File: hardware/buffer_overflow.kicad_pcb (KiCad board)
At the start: 2 copper layers, 33.1 x 30.1 mm, 19 parts, among them J1 E1, U1 LM741

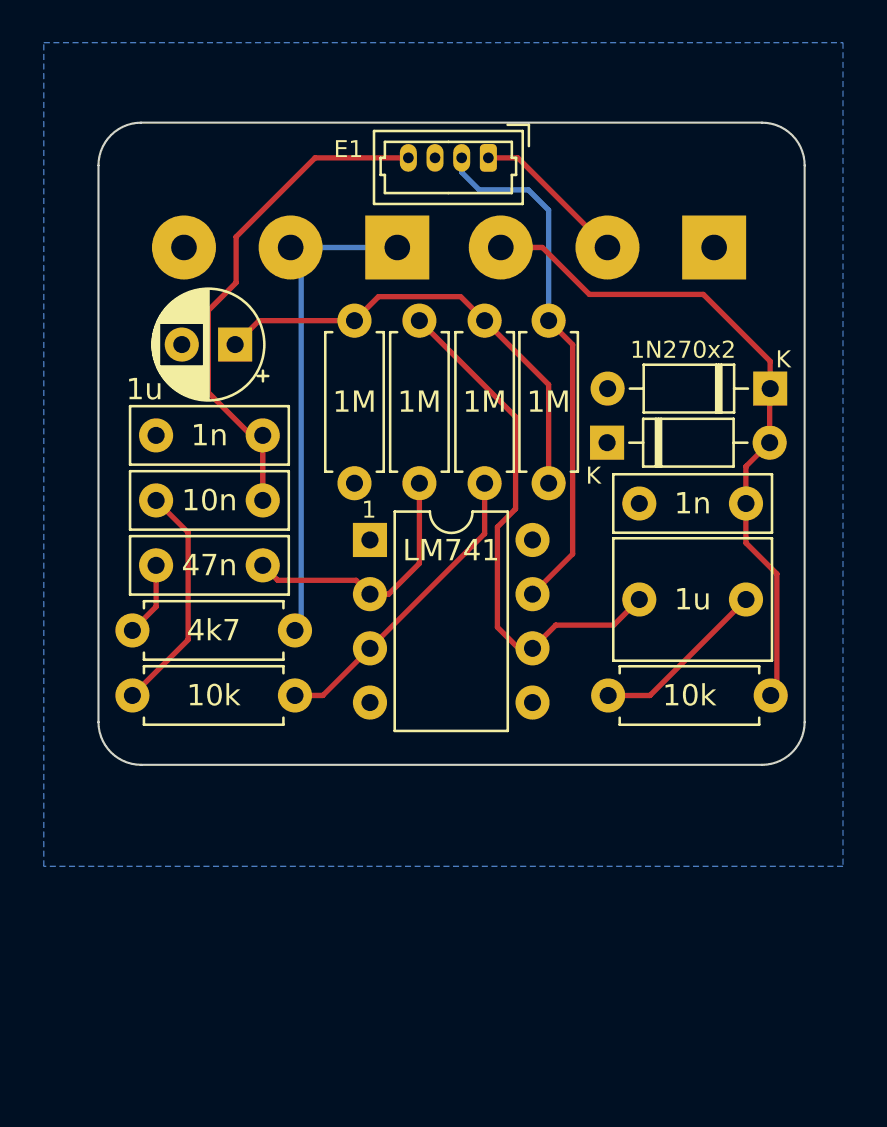
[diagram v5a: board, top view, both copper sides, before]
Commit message: Some updates based on feedback from freestompboxes.org folks:
 - Add back thermal reliefs on ground pads
 - Switch to stereo jacks for improved mechanical support
 - Add 3D models for various parts (courtesy of Vasily Kashirin - https://grabcad.com/vasily.kashirin-1/models?page=1)
 - Add more space between potentiometers (need to update the courtyard to make this more obvious in the future)
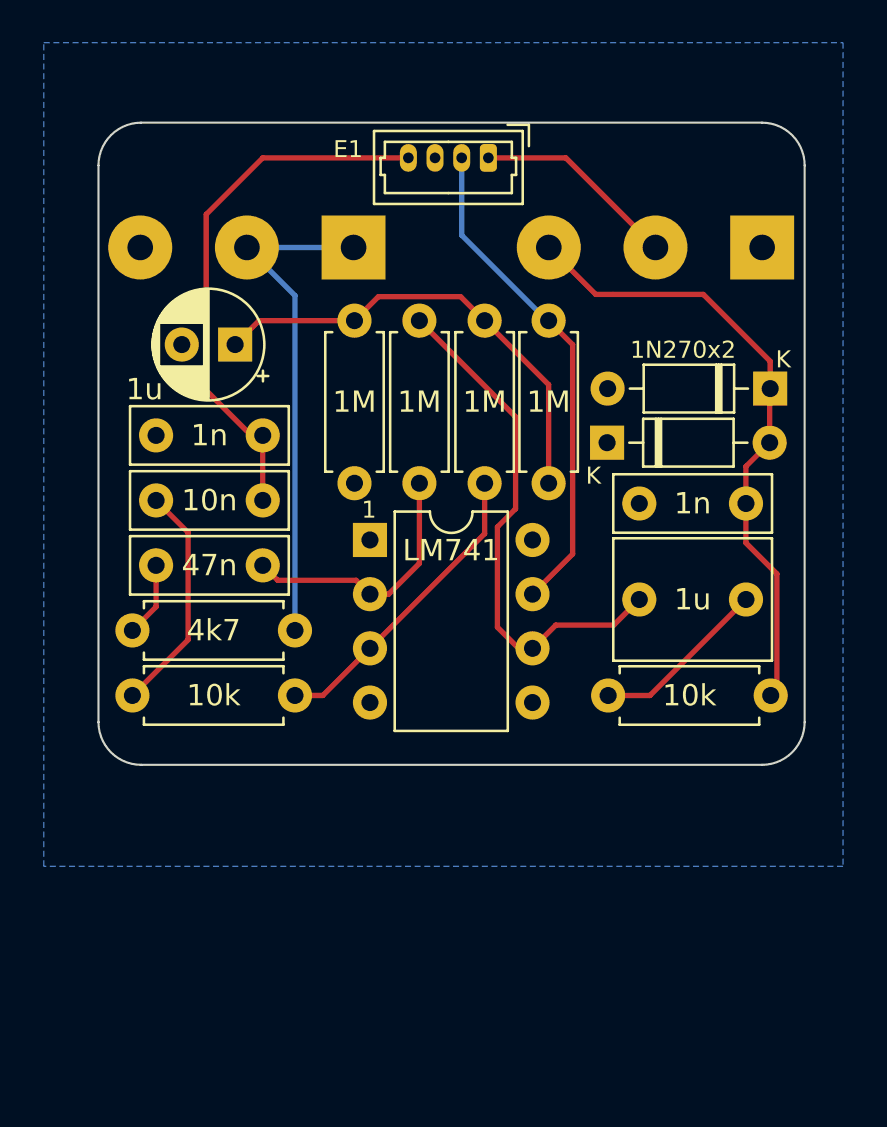
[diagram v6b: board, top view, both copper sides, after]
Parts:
- J1: footprint Connector_Molex:Molex_PicoBlade_53047-0410_1x04_P1.25mm_Vertical -> buffer_overflow:Molex_PicoBlade_53047-0410_1x04_P1.25mm_Vertical_with_3D_Model
- moved POT1 2.25 mm to (71.2, 29.6)
- moved POT2 2.05 mm to (52.0, 29.6)
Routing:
- net /EFFECT_OUT: track 7.32 -> 9.57 mm
- net /PRE_VOLUME: track 31.7 -> 29.5 mm
- net /EFFECT_IN: track 23.9 -> 25.4 mm
- net /9V0: track 24.7 -> 23.4 mm
- net /GAIN_CTL: track 23.4 -> 24.6 mm
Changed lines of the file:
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@@
   (title_block
     (title "Buffer Overflow Drive Effect")
-    (date "2023-03-03")
-    (rev "v0.38")
+    (date "2023-03-04")
+    (rev "v0.39")
     (comment 1 " github.com/whbeers/buffer_overflow")
   )
@@
     )
   )
-  (footprint "Connector_Molex:Molex_PicoBlade_53047-0410_1x04_P1.25mm_Vertical" (layer "F.Cu")
+  (footprint "buffer_overflow:Molex_PicoBlade_53047-0410_1x04_P1.25mm_Vertical_with_3D_Model" (layer "F.Cu")
     (at 63.375 29.25 180)
     (descr "Molex PicoBlade Connector System, 53047-0410, 4 Pins per row (http://www.molex.com/pdm_docs/sd/530470610_sd.pdf), generated with kicad-footprint-generator")
@@
     (property "ki_keywords" "connector")
     (attr through_hole)
-    (fp_text reference "J1" (at 1.88 -3.25) (layer "F.Fab")
-        (effects (font (size 1 1) (thickness 0.15)))
-    )
-    (fp_text value "E1" (at 6.555113 0.399999) (layer "F.SilkS" knockout)
+    (fp_text reference "J1" (at 1.88 -3.25 180) (layer "F.Fab")
+        (effects (font (size 1 1) (thickness 0.15)))
+    )
+    (fp_text value "E1" (at 6.575 0.4 180) (layer "F.SilkS" knockout)
         (effects (font (size 0.8 0.8) (thickness 0.15)))
     )
-    (fp_text user "${REFERENCE}" (at 1.88 -1.35) (layer "F.Fab")
+    (fp_text user "${REFERENCE}" (at 1.88 -1.35 180) (layer "F.Fab")
         (effects (font (size 1 1) (thickness 0.15)))
     )
@@
       (rotate (xyz 0 0 0))
     )
+    (model "/home/whbeers/src-mine/stepfiles/530470410.stp"
+      (offset (xyz 1.9 -1.15 5.5))
+      (scale (xyz 1 1 1))
+      (rotate (xyz 90 0 0))
+    )
   )
   (footprint "Resistor_THT:R_Axial_DIN0207_L6.3mm_D2.5mm_P7.62mm_Horizontal" (layer "F.Cu")
@@
   )
   (footprint "buffer_overflow:Potentiometer_Single_3_Horizontal" (layer "B.Cu")
-    (at 68.95 29.64 180)
+    (at 71.2 29.64 180)
     (property "Label" "Volume")
     (property "Sheetfile" "buffer_overflow.kicad_sch")
@@
     (property "ki_keywords" "resistor variable")
     (attr through_hole)
-    (fp_text reference "POT1" (at -0.0075 -7.06 unlocked) (layer "B.Fab" knockout)
+    (fp_text reference "POT1" (at -0.0075 -7.06 unlocked) (layer "B.Fab")
         (effects (font (size 1 1) (thickness 0.15)) (justify mirror))
     )
@@
         (effects (font (size 0.8 0.8) (thickness 0.15)) (justify mirror))
     )
-    (fp_text user "Vol" (at -7.75 -4.41 270 unlocked) (layer "B.SilkS" knockout)
+    (fp_text user "Vol" (at -5.5 -6.61 unlocked) (layer "B.SilkS" knockout)
         (effects (font (size 0.8 0.8) (thickness 0.15)) (justify mirror))
     )
@@
     (pad "3" thru_hole circle (at 4.9925 -3.81 270) (size 3 3) (drill 1.2) (layers "*.Cu" "*.Mask")
       (net 9 "/PRE_VOLUME") (pinfunction "3") (pintype "passive"))
+    (model "/home/whbeers/src-mine/stepfiles/RV16AF-41.step"
+      (offset (xyz 0 12.2 0.5))
+      (scale (xyz 1 1 1))
+      (rotate (xyz 0 0 0))
+    )
   )
   (footprint "buffer_overflow:Potentiometer_Single_3_Horizontal" (layer "B.Cu")
-    (at 54.1 29.64 180)
+    (at 52.05 29.64 180)
     (property "Label" "Gain")
     (property "Sheetfile" "buffer_overflow.kicad_sch")
@@
     (property "ki_keywords" "resistor variable")
     (attr through_hole)
-    (fp_text reference "POT2" (at 0 -7.06 unlocked) (layer "B.Fab" knockout)
+    (fp_text reference "POT2" (at 0 -7.06 unlocked) (layer "B.Fab")
         (effects (font (size 1 1) (thickness 0.15)) (justify mirror))
     )
@@
         (effects (font (size 0.8 0.8) (thickness 0.15)) (justify mirror))
     )
-    (fp_text user "Gain" (at 7.65 -3.61 90 unlocked) (layer "B.SilkS" knockout)
+    (fp_text user "Gain" (at 5.1 -6.56 unlocked) (layer "B.SilkS" knockout)
         (effects (font (size 0.8 0.8) (thickness 0.15)) (justify mirror))
     )
@@
     (pad "3" thru_hole circle (at 4.9925 -3.81 270) (size 3 3) (drill 1.2) (layers "*.Cu" "*.Mask")
       (net 1 "GND") (pinfunction "3") (pintype "passive"))
+    (model "/home/whbeers/src-mine/stepfiles/RV16AF-41.step"
+      (offset (xyz 0 12.2 0.5))
+      (scale (xyz 1 1 1))
+      (rotate (xyz 0 0 0))
+    )
   )
   (gr_arc (start 45.1 29.6) (mid 45.685786 28.185786) (end 47.1 27.6)
@@
   (segment (start 70.95 54.45) (end 75.45 49.95) (width 0.25) (layer "F.Cu") (net 4))
   (segment (start 68.99 54.45) (end 70.95 54.45) (width 0.25) (layer "F.Cu") (net 4))
-  (segment (start 51.55 32.95) (end 51.55 35.1) (width 0.25) (layer "F.Cu") (net 5))
-  (segment (start 50.25 36.4) (end 50.25 40.25) (width 0.25) (layer "F.Cu") (net 5))
+  (segment (start 59.625 29.25) (end 52.8 29.25) (width 0.25) (layer "F.Cu") (net 5))
+  (segment (start 50.15 31.9) (end 50.15 40.15) (width 0.25) (layer "F.Cu") (net 5))
   (segment (start 52.8 42.258) (end 52.8 45.306) (width 0.25) (layer "F.Cu") (net 5))
-  (segment (start 51.55 35.1) (end 50.25 36.4) (width 0.25) (layer "F.Cu") (net 5))
-  (segment (start 55.25 29.25) (end 51.55 32.95) (width 0.25) (layer "F.Cu") (net 5))
-  (segment (start 59.625 29.25) (end 55.25 29.25) (width 0.25) (layer "F.Cu") (net 5))
-  (segment (start 50.25 40.25) (end 52.258 42.258) (width 0.25) (layer "F.Cu") (net 5))
+  (segment (start 52.8 29.25) (end 50.15 31.9) (width 0.25) (layer "F.Cu") (net 5))
   (segment (start 52.258 42.258) (end 52.8 42.258) (width 0.25) (layer "F.Cu") (net 5))
+  (segment (start 50.15 40.15) (end 52.258 42.258) (width 0.25) (layer "F.Cu") (net 5))
   (segment (start 46.69 54.448) (end 49.3 51.838) (width 0.25) (layer "F.Cu") (net 6))
   (segment (start 49.3 51.838) (end 49.3 46.806) (width 0.25) (layer "F.Cu") (net 6))
@@
   (segment (start 66.535 51.15) (end 65.445 52.24) (width 0.25) (layer "F.Cu") (net 8))
   (segment (start 64.65 45.7) (end 63.8 46.55) (width 0.25) (layer "F.Cu") (net 8))
-  (segment (start 65.909009 33.45) (end 63.9575 33.45) (width 0.25) (layer "F.Cu") (net 9))
   (segment (start 73.45 35.65) (end 76.585 38.785) (width 0.25) (layer "F.Cu") (net 9))
   (segment (start 76.56 40.09) (end 76.585 40.065) (width 0.25) (layer "F.Cu") (net 9))
   (segment (start 75.45 45.45) (end 75.45 47.3) (width 0.25) (layer "F.Cu") (net 9))
+  (segment (start 66.2075 33.45) (end 68.4075 35.65) (width 0.25) (layer "F.Cu") (net 9))
   (segment (start 76.56 42.6) (end 76.56 40.09) (width 0.25) (layer "F.Cu") (net 9))
   (segment (start 76.585 38.785) (end 76.585 40.065) (width 0.25) (layer "F.Cu") (net 9))
-  (segment (start 73.45 35.65) (end 68.109009 35.65) (width 0.25) (layer "F.Cu") (net 9))
+  (segment (start 68.4075 35.65) (end 69.2 35.65) (width 0.25) (layer "F.Cu") (net 9))
   (segment (start 75.45 43.71) (end 75.45 45.45) (width 0.25) (layer "F.Cu") (net 9))
+  (segment (start 73.45 35.65) (end 69.2 35.65) (width 0.25) (layer "F.Cu") (net 9))
   (segment (start 76.56 42.6) (end 75.45 43.71) (width 0.25) (layer "F.Cu") (net 9))
   (segment (start 76.9 48.75) (end 76.9 54.2) (width 0.25) (layer "F.Cu") (net 9))
@@
   (segment (start 76.9 54.2) (end 76.65 54.45) (width 0.25) (layer "F.Cu") (net 9))
   (segment (start 76.61 54.45) (end 76.65 54.45) (width 0.25) (layer "F.Cu") (net 9))
-  (segment (start 68.109009 35.65) (end 65.909009 33.45) (width 0.25) (layer "F.Cu") (net 9))
+  (segment (start 52.0575 33.45) (end 57.0575 33.45) (width 0.25) (layer "B.Cu") (net 10))
   (segment (start 54.6 50.912) (end 54.11 51.402) (width 0.25) (layer "B.Cu") (net 10))
-  (segment (start 54.1075 33.45) (end 54.6 33.9425) (width 0.25) (layer "B.Cu") (net 10))
-  (segment (start 59.1075 33.45) (end 54.1075 33.45) (width 0.25) (layer "B.Cu") (net 10))
-  (segment (start 54.6 33.9425) (end 54.6 50.912) (width 0.25) (layer "B.Cu") (net 10))
+  (segment (start 54.31 51.4) (end 54.31 35.7025) (width 0.25) (layer "B.Cu") (net 10))
+  (segment (start 54.31 35.7025) (end 52.0575 33.45) (width 0.25) (layer "B.Cu") (net 10))
   (segment (start 58.7 49.7) (end 57.825 49.7) (width 0.25) (layer "F.Cu") (net 11))
   (segment (start 57.175 49.05) (end 57.825 49.7) (width 0.25) (layer "F.Cu") (net 11))
@@
   (segment (start 67.325 47.82) (end 65.445 49.7) (width 0.25) (layer "F.Cu") (net 12))
   (segment (start 66.2 36.88) (end 67.325 38.005) (width 0.25) (layer "F.Cu") (net 12))
-  (segment (start 62.125 29.25) (end 62.125 29.925) (width 0.25) (layer "B.Cu") (net 12))
-  (segment (start 62.95 30.75) (end 65.25 30.75) (width 0.25) (layer "B.Cu") (net 12))
-  (segment (start 62.125 29.925) (end 62.95 30.75) (width 0.25) (layer "B.Cu") (net 12))
-  (segment (start 65.25 30.75) (end 66.2 31.7) (width 0.25) (layer "B.Cu") (net 12))
-  (segment (start 66.2 31.7) (end 66.2 36.88) (width 0.25) (layer "B.Cu") (net 12))
-  (segment (start 64.7575 29.25) (end 68.9575 33.45) (width 0.25) (layer "F.Cu") (net 13))
-  (segment (start 63.375 29.25) (end 64.7575 29.25) (width 0.25) (layer "F.Cu") (net 13))
+  (segment (start 62.125 29.25) (end 62.125 32.875) (width 0.25) (layer "B.Cu") (net 12))
+  (segment (start 66.13 36.88) (end 66.2 36.88) (width 0.25) (layer "B.Cu") (net 12))
+  (segment (start 62.125 32.875) (end 66.13 36.88) (width 0.25) (layer "B.Cu") (net 12))
+  (segment (start 67.0075 29.25) (end 71.2075 33.45) (width 0.25) (layer "F.Cu") (net 13))
+  (segment (start 63.375 29.25) (end 67.0075 29.25) (width 0.25) (layer "F.Cu") (net 13))
   (zone (net 1) (net_name "GND") (layer "B.Cu") (hatch edge 0.5)
-    (connect_pads yes (clearance 0.508))
+    (connect_pads thru_hole_only (clearance 0.508))
     (min_thickness 0.25) (filled_areas_thickness no)
     (fill yes (thermal_gap 0.5) (thermal_bridge_width 0.5))
@@
     )
   )
-  (group "" (id ebcc14d2-dbee-420a-b855-523dddbd1c6e)
-    (members
-      3ab789d6-250c-4083-a1c4-6b810d459a77
-      e8914e6e-2997-436a-8149-3f8dae69216a
-    )
-  )

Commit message: fix a couple DRCs
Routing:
- net /GAIN_CTL: track 24.6 -> 23.9 mm
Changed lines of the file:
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@@
       (rotate (xyz 0 0 0))
     )
-    (model "/home/whbeers/src-mine/stepfiles/530470410.stp"
+    (model "${KIPRJMOD}/buffer_overflow.pretty/530470410.stp"
       (offset (xyz 1.9 -1.15 5.5))
       (scale (xyz 1 1 1))
@@
     (pad "3" thru_hole circle (at 4.9925 -3.81 270) (size 3 3) (drill 1.2) (layers "*.Cu" "*.Mask")
       (net 9 "/PRE_VOLUME") (pinfunction "3") (pintype "passive"))
-    (model "/home/whbeers/src-mine/stepfiles/RV16AF-41.step"
+    (model "${KIPRJMOD}/buffer_overflow.pretty/RV16AF-41.step"
       (offset (xyz 0 12.2 0.5))
       (scale (xyz 1 1 1))
@@
     (pad "3" thru_hole circle (at 4.9925 -3.81 270) (size 3 3) (drill 1.2) (layers "*.Cu" "*.Mask")
       (net 1 "GND") (pinfunction "3") (pintype "passive"))
-    (model "/home/whbeers/src-mine/stepfiles/RV16AF-41.step"
+    (model "${KIPRJMOD}/buffer_overflow.pretty/RV16AF-41.step"
       (offset (xyz 0 12.2 0.5))
       (scale (xyz 1 1 1))
@@
   (segment (start 76.61 54.45) (end 76.65 54.45) (width 0.25) (layer "F.Cu") (net 9))
   (segment (start 52.0575 33.45) (end 57.0575 33.45) (width 0.25) (layer "B.Cu") (net 10))
-  (segment (start 54.6 50.912) (end 54.11 51.402) (width 0.25) (layer "B.Cu") (net 10))
   (segment (start 54.31 51.4) (end 54.31 35.7025) (width 0.25) (layer "B.Cu") (net 10))
   (segment (start 54.31 35.7025) (end 52.0575 33.45) (width 0.25) (layer "B.Cu") (net 10))
